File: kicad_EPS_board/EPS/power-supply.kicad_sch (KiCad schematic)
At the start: 18 parts, among them T2 BC846B, T3 BC846B, T4 BC856B, U12 TSR 0.5-24120SM

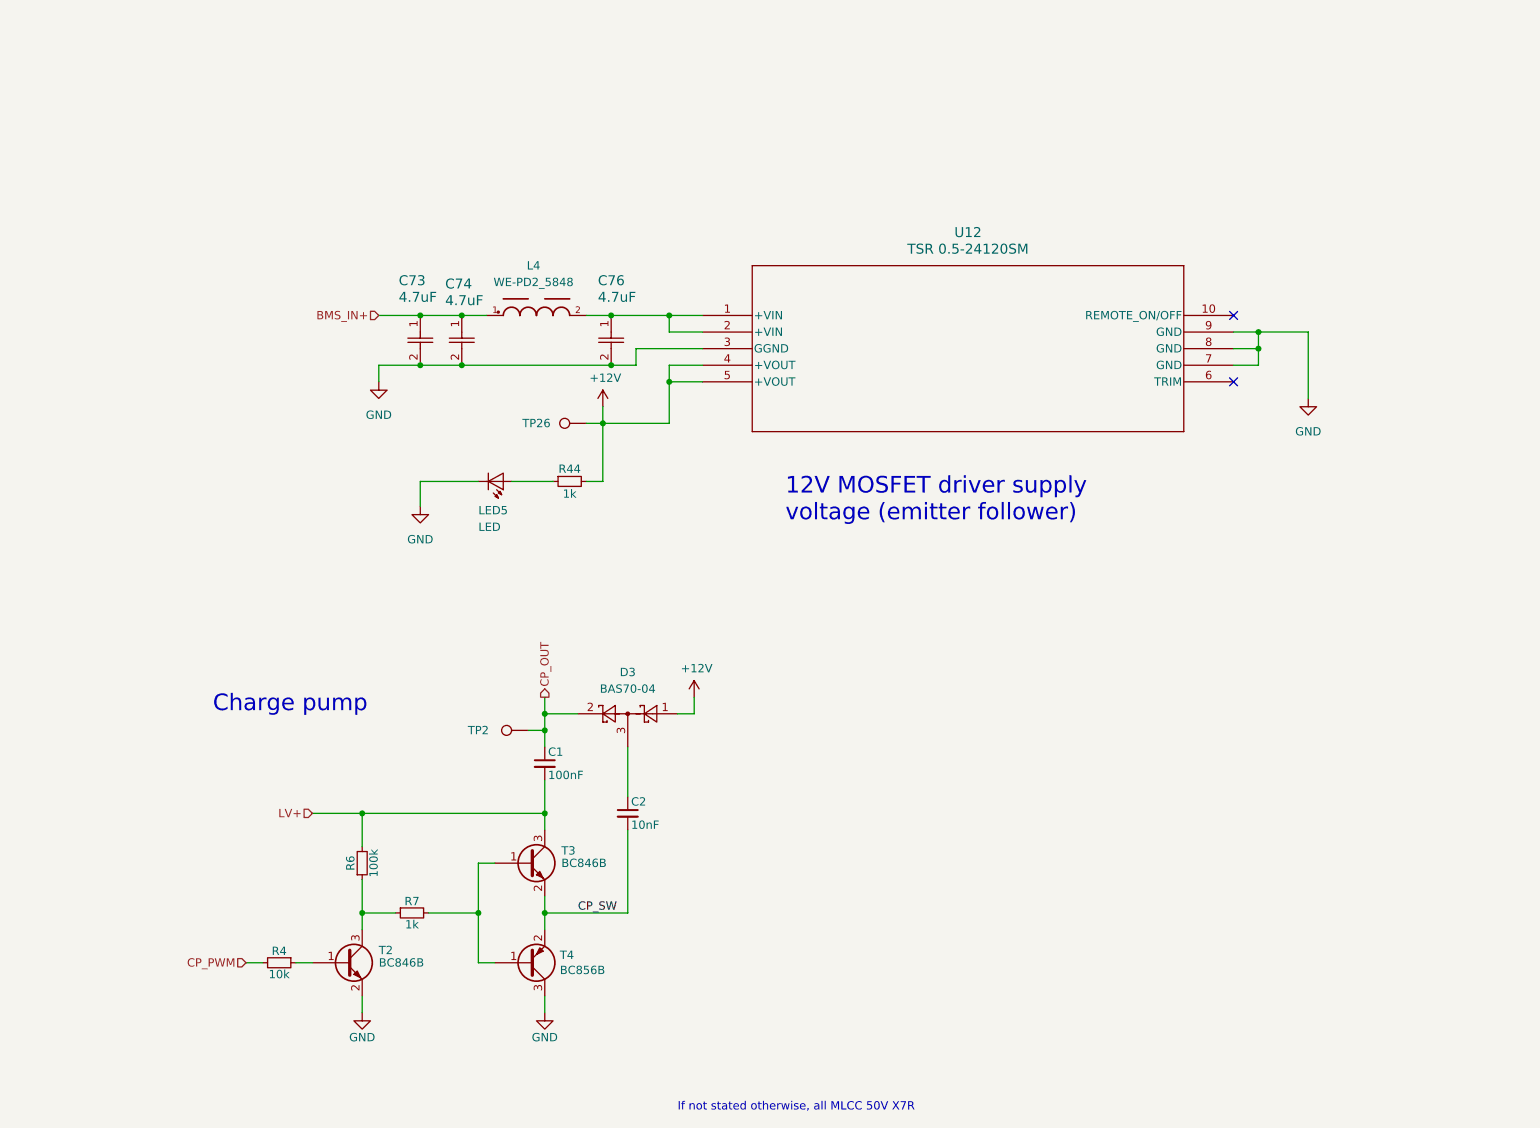
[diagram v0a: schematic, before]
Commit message: kicad EPS board V2 revision and already generated html doc files
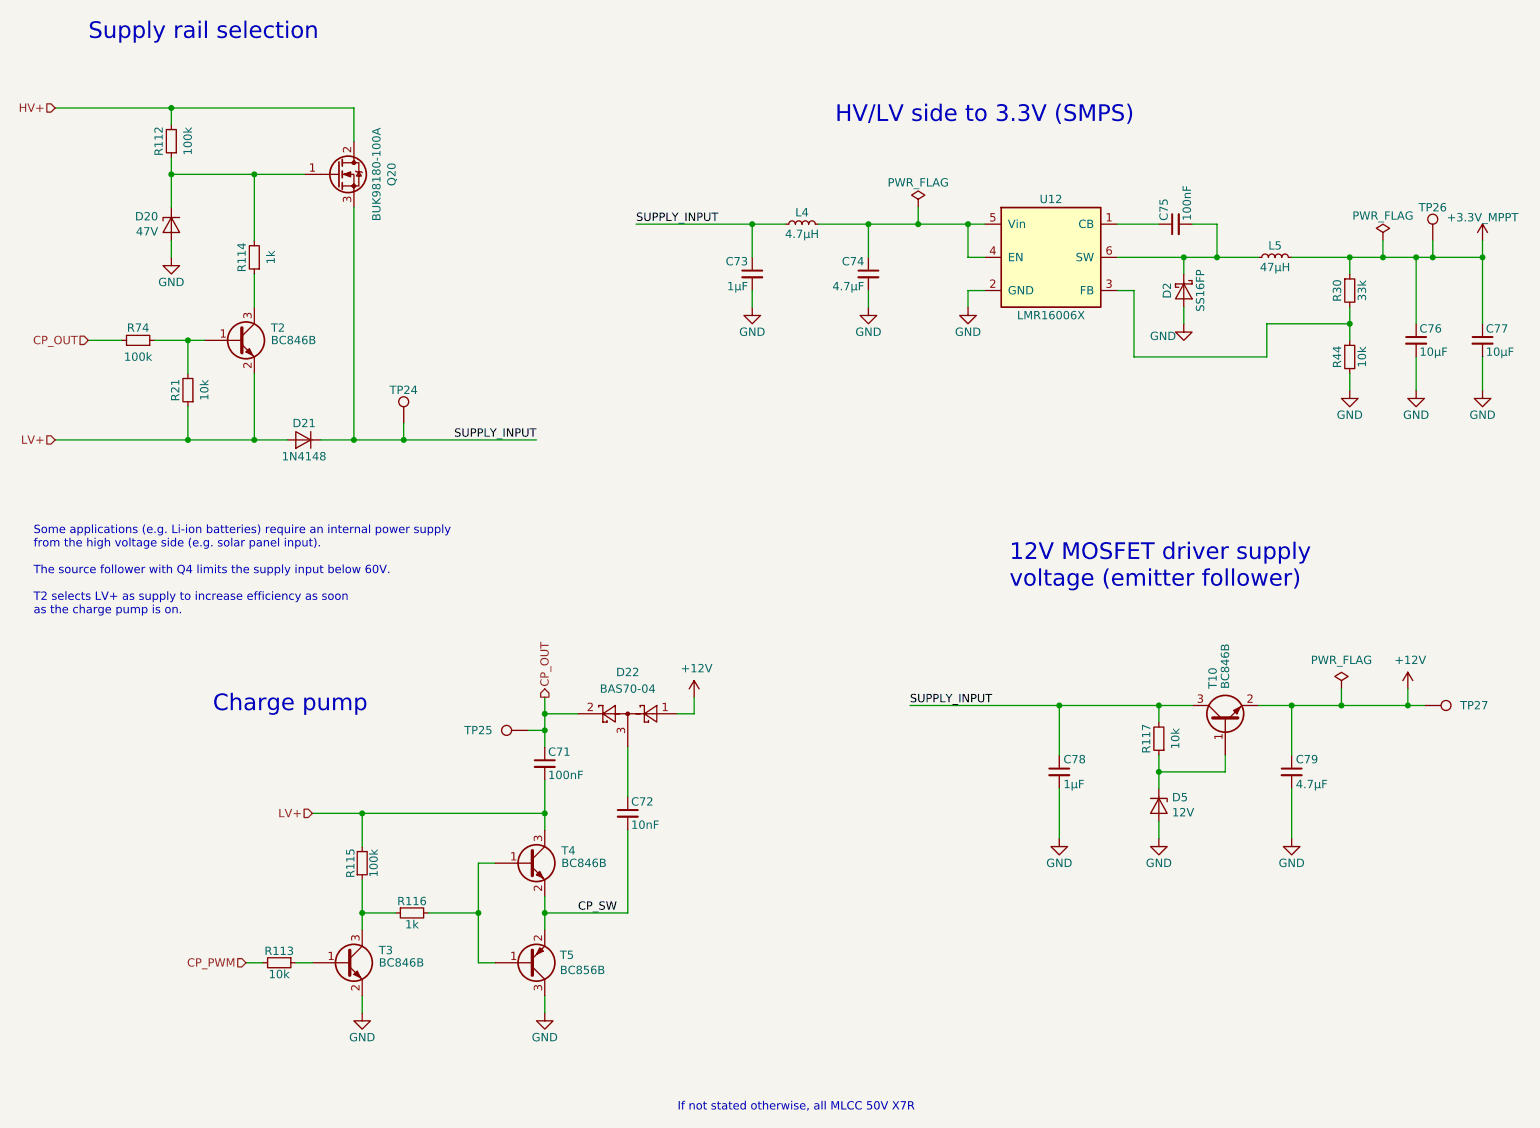
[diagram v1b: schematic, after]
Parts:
- removed C73, C74, C76: 4.7uF, LibreSolar:CAPC370195_195N_KEM, symbol C1206X475J5RACAUTO:C1206X475J5RACAUTO
- removed L4: WE-PD2_5848, LibreSolar:WE-PD2_5848, symbol WE-PD2_5848:WE-PD2_5848
- removed LED5: LED, LibreSolar:LED_0603_D3.0mm, symbol Project:D_LED
- removed U12: TSR 0.5-24120SM, LibreSolar:TSR 0.5SM_TRP, symbol TSR 0.5-24120SM:TSR_0.5-24120SM
- added C73: 1µF, LibreSolar:C_0805_2012, symbol Project:C
- added C74: 4.7µF, LibreSolar:C_1210_3225, symbol Project:C
- added C75: 100nF, LibreSolar:C_0603_1608, symbol Project:C
- added C76, C77: 10µF, LibreSolar:C_0805_2012, symbol Project:C
- added C78: 1µF, LibreSolar:C_0603_1608, symbol Project:C
- added C79: 4.7µF, LibreSolar:C_0603_1608, symbol Project:C
- added D2: SS16FP, Diode_SMD:D_PowerDI-123, symbol Project:D_Schottky
- added D20: 47V, Diode_SMD:D_SOT-23_ANK, symbol Project:D_Zener
- added D21: 1N4148, LibreSolar:D_SOD-123, symbol Project:D
- added D5: 12V, Diode_SMD:D_SOT-23_ANK, symbol Project:D_Zener
- added L4: 4.7µH, Inductor_SMD:L_0805_2012Metric, symbol Device:L_Small
- added L5: 47µH, LibreSolar:Bourns_SRN6045TA, symbol Device:L_Small
- added Q20: BUK98180-100A, Package_TO_SOT_SMD:SOT-223-3_TabPin2, symbol Device:Q_NMOS_GDS
- added R112, R74: 100k, LibreSolar:R_0603_1608, symbol Project:R
- added R114: 1k, LibreSolar:R_0603_1608, symbol Project:R
- added R117, R21: 10k, LibreSolar:R_0603_1608, symbol Project:R
- added R30: 33k, LibreSolar:R_0603_1608, symbol Project:R
- added T10, T2: BC846B, LibreSolar:SOT-23, symbol Transistor_BJT:BC846
- added TP24, TP27: 1.5mm, TestPoint:TestPoint_Pad_D1.5mm, symbol Connector:TestPoint
- added U12: LMR16006X, LibreSolar:SOT-23-6, symbol Project:LMR16006
- R44: value 1k -> 10k; Manufacturer Yageo -> any; PartNumber RC0603FR-071KL -> (none); Remarks (none) -> 1%
- renumbered C1 to C71, C2 to C72, D3 to D22, R4 to R113, R6 to R115, R7 to R116, T2 to T3, T3 to T4, T4 to T5, TP2 to TP25
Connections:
- net +12V: now also C79.1, T10.2 (E), TP27.1; no longer R44.2, TP26.1
- net CP_OUT: now also R74.2
- net GND: now also R44.2, C73.2, C74.2, C76.2, C77.2, C78.2, C79.2, D2.2 (A), D20.2 (A), D5.2 (A), U12.2 (GND)
- net LV+: now also D21.2 (A), R21.1, T2.2 (E)
- net at R44.1: now also R30.2, U12.3 (FB)
- new net: D5.1 (K), R117.1, T10.1 (B)
- new net: R21.2, R74.1, T2.1 (B)
- new net: R114.1, T2.3 (C)
- new net: C75.2, D2.1 (K), L5.1, U12.6 (SW)
- new net: C75.1, U12.1 (CB)
- new net: C74.1, L4.2, U12.4 (EN), U12.5 (Vin)
- new net: D20.1 (K), Q20.1 (G), R112.1, R114.2
- new net +3.3V_MPPT: C76.1, C77.1, L5.2, R30.1, TP26.1
- new net HV+: Q20.2 (D), R112.2
- new net SUPPLY_INPUT: C73.1, C78.1, D21.1 (K), L4.1, Q20.3 (S), R117.2, T10.3 (C), TP24.1
- no-connect marks 2 -> 0
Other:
- note added: "HV/LV side to 3.3V (SMPS)"
- note added: "Some applications (e.g. Li-ion batteries) require an internal power supply from the high voltage side (e.g. solar panel input). The source follower with Q4 limits the supply input below 60V. T2 selects LV+ as supply to increase efficiency as soon as the charge pump is on."
- note added: "Supply rail selection"
